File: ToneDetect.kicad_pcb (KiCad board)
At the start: 2 copper layers, 177.8 x 50.8 mm, 45 parts, among them J1 XLR3, J2 Conn_01x02_Male, SW1 SW_SPST, SW2 SW_SPST, SW3 SW_SPST, SW4 SW_SPST, SW5 SW_SPST, SW6 SW_SPST, U1 74HCT04, U2 74HCT04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

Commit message: tweaks to schematic and layout
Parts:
- added R18: 10k, Resistor_THT:R_Axial_DIN0204_L3.6mm_D1.6mm_P5.08mm_Horizontal, F.Cu at (210.8, 78.7)
- added R19: 10k, Resistor_THT:R_Axial_DIN0204_L3.6mm_D1.6mm_P5.08mm_Horizontal, F.Cu at (203.2, 78.7)
- moved U2 64.4 mm to (174.0, 105.4)
- moved C8 58.3 mm to (181.6, 101.6), turned to 180 degrees
- moved U3 21.9 mm to (143.5, 102.9)
- moved C11 16.6 mm to (151.1, 97.8), turned to 180 degrees
- moved C7 6.35 mm to (121.9, 100.3), turned to 180 degrees
- moved C4 5.08 mm to (162.6, 109.2)
- moved C6 5.08 mm to (221.0, 109.2)
- moved C5 5.08 mm to (193.0, 109.2)
- turned J2 to 90 degrees
- turned R17 to 0 degrees
- renumbered SW6 to SW1, SW5 to SW2, SW4 to SW3, SW3 to SW4, SW2 to SW5, SW1 to SW6
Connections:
- U1 pad 11: Net-(C5-Pad1) -> Net-(C3-Pad1)
- U1 pad 13: Net-(C6-Pad1) -> Net-(U1-Pad13)
- U1 pad 2: Net-(U1-Pad2) -> Net-(U1-Pad13)
- U1 pad 3: Net-(C2-Pad1) -> Net-(U1-Pad3)
- U1 pad 5: Net-(C3-Pad1) -> Net-(C2-Pad1)
- U1 pad 6: Net-(U1-Pad6) -> Net-(U1-Pad3)
- U1 pad 9: Net-(C4-Pad1) -> Net-(U1-Pad10)
- U2 pad 1: Net-(U1-Pad2) -> Net-(C4-Pad1)
- U2 pad 11: Net-(U1-Pad10) -> Net-(U2-Pad11)
- U2 pad 13: Net-(U1-Pad12) -> Net-(U2-Pad13)
- U2 pad 3: Net-(U1-Pad4) -> Net-(U2-Pad2)
- U2 pad 5: Net-(U1-Pad6) -> Net-(C5-Pad1)
- U2 pad 6: Net-(U2-Pad6) -> Net-(U2-Pad11)
- U2 pad 8: Net-(U2-Pad8) -> Net-(U2-Pad13)
- U2 pad 9: Net-(U1-Pad8) -> Net-(C6-Pad1)
- U3 pad 1: Net-(U2-Pad10) -> Net-(U1-Pad4)
- U3 pad 10: Net-(U2-Pad2) -> Net-(U2-Pad12)
- U3 pad 11: Net-(U2-Pad4) -> Net-(U2-Pad10)
- U3 pad 12: Net-(U2-Pad6) -> Net-(U2-Pad4)
- U3 pad 13: Net-(U2-Pad8) -> Net-(U1-Pad8)
- U3 pad 2: Net-(U2-Pad12) -> Net-(U1-Pad12)
- U5 pad 5: +5V -> Net-(R18-Pad2)
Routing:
- net +5V: track 410.6 -> 5.52 mm
- net Net-(C5-Pad1): track 84.1 -> 10.8 mm
- net Net-(C6-Pad1): track 112.9 -> 61.0 mm
- net Net-(U1-Pad6): track 37.0 -> 0.00 mm
- net Net-(U1-Pad4): track 33.3 -> 0.40 mm
- net Net-(C4-Pad1): track 57.5 -> 27.6 mm
- net Net-(U1-Pad2): track 28.0 -> 0.00 mm
- net Net-(U1-Pad12): track 0.00 -> 23.2 mm
- net Net-(U1-Pad8): track 31.3 -> 41.8 mm
- net Net-(R18-Pad2): track 0.00 -> 9.07 mm
- net Net-(U1-Pad13): track 0.00 -> 8.02 mm
- net Net-(C3-Pad1): track 33.7 -> 26.8 mm
- net Net-(C2-Pad1): track 20.9 -> 16.8 mm
- net Net-(U1-Pad10): track 0.00 -> 2.54 mm
- net Net-(U1-Pad3): track 0.00 -> 1.20 mm
- added copper zone on F.Cu, net +5V
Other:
- outline, holes or cut-outs redrawn

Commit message: tweak design
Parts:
- C1, C14, C2, C3, C4, C5, C6: footprint Capacitors_THT:CP_Radial_D5.0mm_P2.50mm -> Capacitor_THT:CP_Radial_D5.0mm_P2.50mm
- C10, C11, C12, C13, C7, C8, C9: footprint Capacitors_THT:C_Disc_D3.8mm_W2.6mm_P2.50mm -> Capacitor_THT:C_Disc_D3.8mm_W2.6mm_P2.50mm
- moved R17 22.9 mm to (193.0, 82.5)
- moved C14 10.9 mm to (194.3, 88.9), turned to 90 degrees
- moved C13 6.48 mm to (204.5, 97.8)
- moved R16 6.48 mm to (214.6, 97.8)
- moved R15 6.48 mm to (214.6, 87.6)
- moved U5 6.48 mm to (199.4, 92.7)
- moved C11 6.37 mm to (154.9, 102.9), turned to 0 degrees
- moved C4 6.35 mm to (166.4, 104.1), turned to 90 degrees
- moved C12 2.82 mm to (166.3, 83.8), turned to 180 degrees
- moved C10 2.58 mm to (177.8, 96.5)
- moved R18 1.27 mm to (212.1, 78.7)
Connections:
- U1 pad 12: Net-(U1-Pad12) -> (no net)
- U1 pad 13: Net-(U1-Pad13) -> GND
- U1 pad 2: Net-(U1-Pad13) -> Net-(U1-Pad2)
- U1 pad 3: Net-(U1-Pad3) -> GND
- U1 pad 4: Net-(U1-Pad4) -> (no net)
- U1 pad 6: Net-(U1-Pad3) -> Net-(U1-Pad6)
- U1 pad 8: Net-(U1-Pad8) -> (no net)
- U1 pad 9: Net-(U1-Pad10) -> GND
- U2 pad 3: Net-(U2-Pad2) -> Net-(U2-Pad3)
- U2 pad 6: Net-(U2-Pad11) -> Net-(U2-Pad6)
- U2 pad 8: Net-(U2-Pad13) -> Net-(U2-Pad8)
- U3 pad 1: Net-(U1-Pad4) -> Net-(U1-Pad6)
- U3 pad 10: Net-(U2-Pad12) -> Net-(U2-Pad8)
- U3 pad 11: Net-(U2-Pad10) -> Net-(U2-Pad6)
- U3 pad 12: Net-(U2-Pad4) -> Net-(U2-Pad2)
- U3 pad 13: Net-(U1-Pad8) -> Net-(U1-Pad10)
- U3 pad 2: Net-(U1-Pad12) -> Net-(U1-Pad2)
- U3 pad 6: Net-(U3-Pad6) -> Net-(U2-Pad3)
- U3 pad 7: Net-(U3-Pad7) -> Net-(U2-Pad11)
- U3 pad 9: Net-(U3-Pad9) -> Net-(U2-Pad13)
- U4 pad 6: Net-(U3-Pad9) -> Net-(U2-Pad12)
- U4 pad 7: Net-(U3-Pad7) -> Net-(U2-Pad10)
- U4 pad 8: Net-(U3-Pad6) -> Net-(U2-Pad4)
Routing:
- net Net-(U2-Pad13): track 0.00 -> 49.0 mm
- net Net-(U2-Pad11): track 0.00 -> 45.2 mm
- net Net-(U1-Pad10): track 2.54 -> 47.5 mm
- net Net-(C13-Pad2): track 0.00 -> 42.1 mm
- net Net-(U2-Pad3): track 0.00 -> 41.9 mm
- net Net-(U1-Pad8): track 41.8 -> 0.00 mm
- net Net-(U1-Pad6): track 0.00 -> 40.5 mm
- net Net-(U2-Pad4): track 0.00 -> 36.2 mm
- net Net-(U1-Pad2): track 0.00 -> 33.9 mm
- net Net-(U2-Pad8): track 0.00 -> 32.7 mm
- net Net-(U2-Pad10): track 0.00 -> 25.9 mm
- net Net-(U2-Pad2): track 0.00 -> 25.0 mm
- net Net-(U2-Pad6): track 0.00 -> 23.9 mm
- net Net-(U1-Pad12): track 23.2 -> 0.00 mm
- net Net-(C5-Pad1): track 10.8 -> 33.5 mm
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
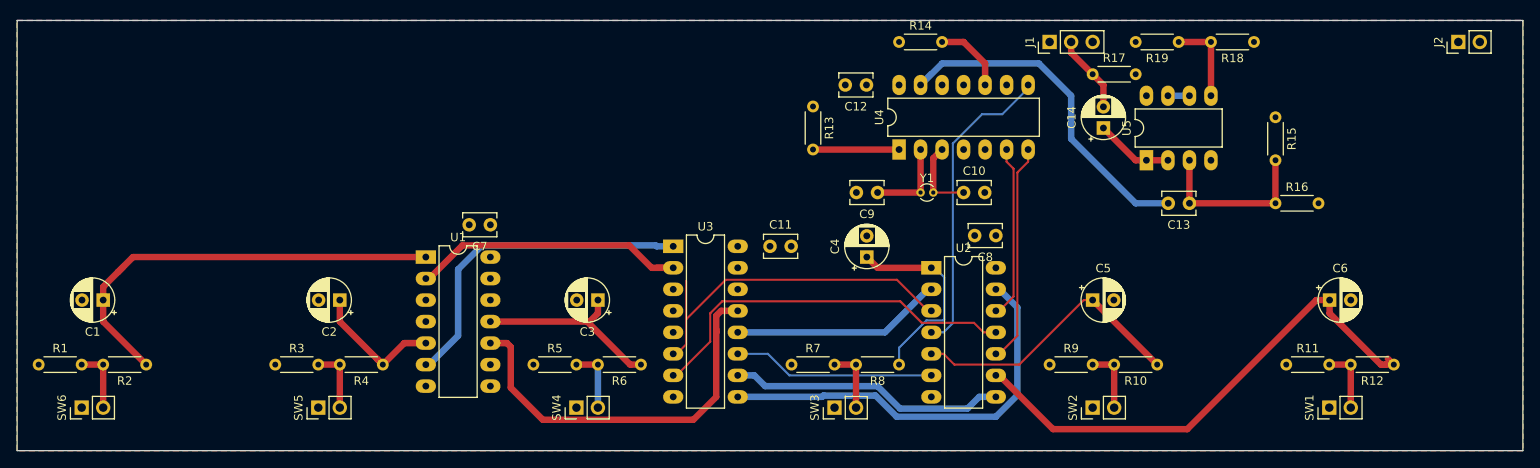
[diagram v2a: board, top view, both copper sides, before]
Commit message: remove a hex inverter and fix up circuit
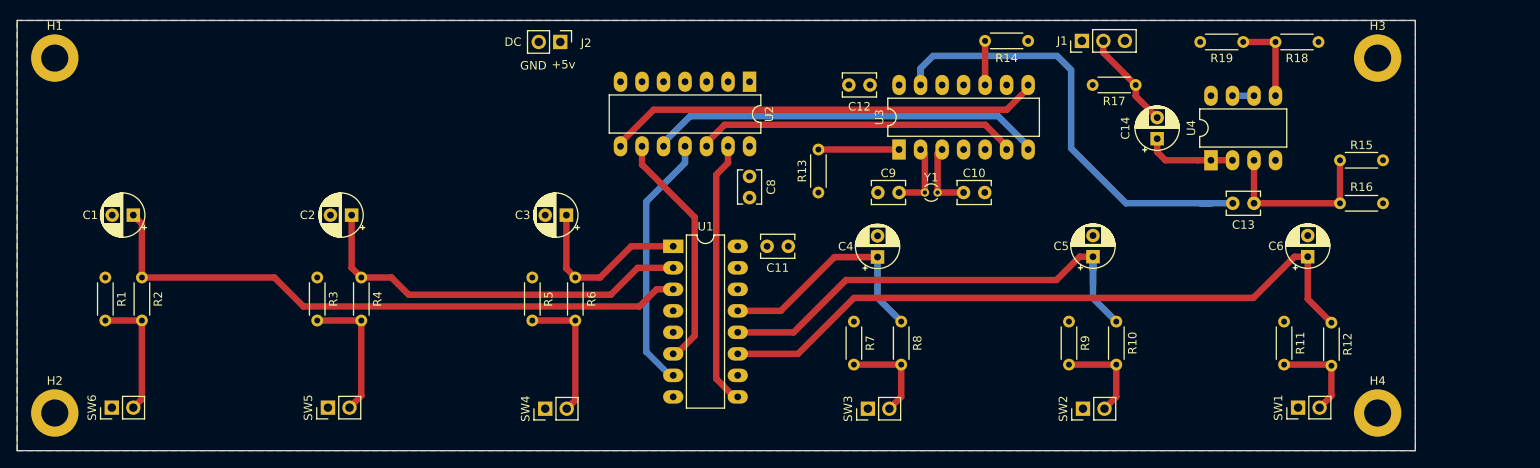
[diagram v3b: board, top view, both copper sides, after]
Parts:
- removed C7: 100nf, Capacitor_THT:C_Disc_D3.8mm_W2.6mm_P2.50mm
- removed the U1 at (114.3, 104.1)
- added H1: M, MountingHole:MountingHole_3.2mm_M3_DIN965_Pad, F.Cu at (70.5, 80.6)
- added H2: M, MountingHole:MountingHole_3.2mm_M3_DIN965_Pad, F.Cu at (70.5, 122.6)
- added H3: M, MountingHole:MountingHole_3.2mm_M3_DIN965_Pad, F.Cu at (226.7, 80.6)
- added H4: M, MountingHole:MountingHole_3.2mm_M3_DIN965_Pad, F.Cu at (226.7, 122.6)
- J2: value Conn_01x02_Male -> DC
- moved J2 106.0 mm to (130.2, 78.7), turned to 270 degrees
- moved U2 30.7 mm to (152.5, 83.4), turned to 270 degrees
- moved C8 29.9 mm to (152.5, 94.6), turned to 270 degrees
- moved R14 15.2 mm to (185.4, 78.6), turned to 180 degrees
- moved R15 13.7 mm to (227.3, 92.7), turned to 180 degrees
- moved R1 13.0 mm to (76.5, 106.6), turned to 270 degrees
- moved R6 12.9 mm to (132.0, 106.6), turned to 270 degrees
- moved R3 11.4 mm to (101.5, 106.6), turned to 270 degrees
- moved C3 10.7 mm to (130.9, 99.2)
- moved C1 10.6 mm to (79.8, 99.2)
- moved R4 10.6 mm to (106.7, 106.6), turned to 270 degrees
- moved R2 10.3 mm to (80.8, 106.6), turned to 270 degrees
- moved R5 10.3 mm to (126.9, 106.6), turned to 270 degrees
- moved R13 10.2 mm to (160.7, 96.5), turned to 90 degrees
- moved C2 10.1 mm to (105.5, 99.2)
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- renumbered U3 to U1, U4 to U3, U5 to U4
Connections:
- C11 pad 1: +5V -> GND
- C11 pad 2: GND -> +5V
- U1 pad 1: Net-(U1-Pad6) -> Net-(C3-Pad1)
- U1 pad 10: Net-(U2-Pad8) -> +5V
- U1 pad 11: Net-(U2-Pad6) -> Net-(C6-Pad1)
- U1 pad 12: Net-(U2-Pad2) -> Net-(C5-Pad1)
- U1 pad 13: Net-(U1-Pad10) -> Net-(C4-Pad1)
- U1 pad 2: Net-(U1-Pad2) -> Net-(C2-Pad1)
- U1 pad 3: GND -> Net-(C1-Pad1)
- U1 pad 4: GND -> +5V
- U1 pad 6: Net-(U2-Pad3) -> Net-(U1-Pad6)
- U2 pad 1: Net-(C4-Pad1) -> GND
- U2 pad 2: Net-(U2-Pad2) -> (no net)
- U2 pad 3: Net-(U2-Pad3) -> GND
- U2 pad 4: Net-(U2-Pad4) -> (no net)
- U2 pad 5: Net-(C5-Pad1) -> GND
- U2 pad 6: Net-(U2-Pad6) -> (no net)
- U2 pad 9: Net-(C6-Pad1) -> Net-(U1-Pad6)
- U3 pad 8: Net-(U2-Pad4) -> Net-(U2-Pad8)
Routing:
- net Net-(U1-Pad10): track 47.5 -> 0.00 mm
- net Net-(U2-Pad3): track 41.9 -> 0.00 mm
- net Net-(U2-Pad4): track 36.2 -> 0.00 mm
- net Net-(U1-Pad2): track 33.9 -> 0.00 mm
- net Net-(C2-Pad1): track 17.2 -> 46.8 mm
- net Net-(C5-Pad1): track 33.5 -> 59.4 mm
- net Net-(U2-Pad2): track 25.0 -> 0.00 mm
- net Net-(U2-Pad6): track 23.9 -> 0.00 mm
- net Net-(U2-Pad10): track 25.9 -> 46.6 mm
- net Net-(C6-Pad1): track 61.0 -> 81.0 mm
- net Net-(C1-Pad1): track 53.3 -> 72.8 mm
- net Net-(U2-Pad8): track 32.7 -> 52.0 mm
- net Net-(U2-Pad12): track 20.5 -> 38.2 mm
- net Net-(U1-Pad9): track 49.0 -> 31.5 mm
- net Net-(U1-Pad7): track 45.2 -> 30.9 mm
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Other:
- board size 177.8 x 50.8 mm -> 165.1 x 50.8 mm
- board text added: "+5v"
- board text added: "GND"
